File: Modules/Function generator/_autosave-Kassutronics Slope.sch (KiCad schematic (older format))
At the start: 127 parts, among them J1 PJ301M-12, J10 Conn_01x08_Female, J11 Conn_01x08_Male, J12 Conn_01x05_Female, J13 Conn_01x05_Male, J14 Conn_01x06_Female, J15 Conn_01x06_Male, J2 PJ301M-12, J3 PJ301M-12, J4 PJ301M-12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

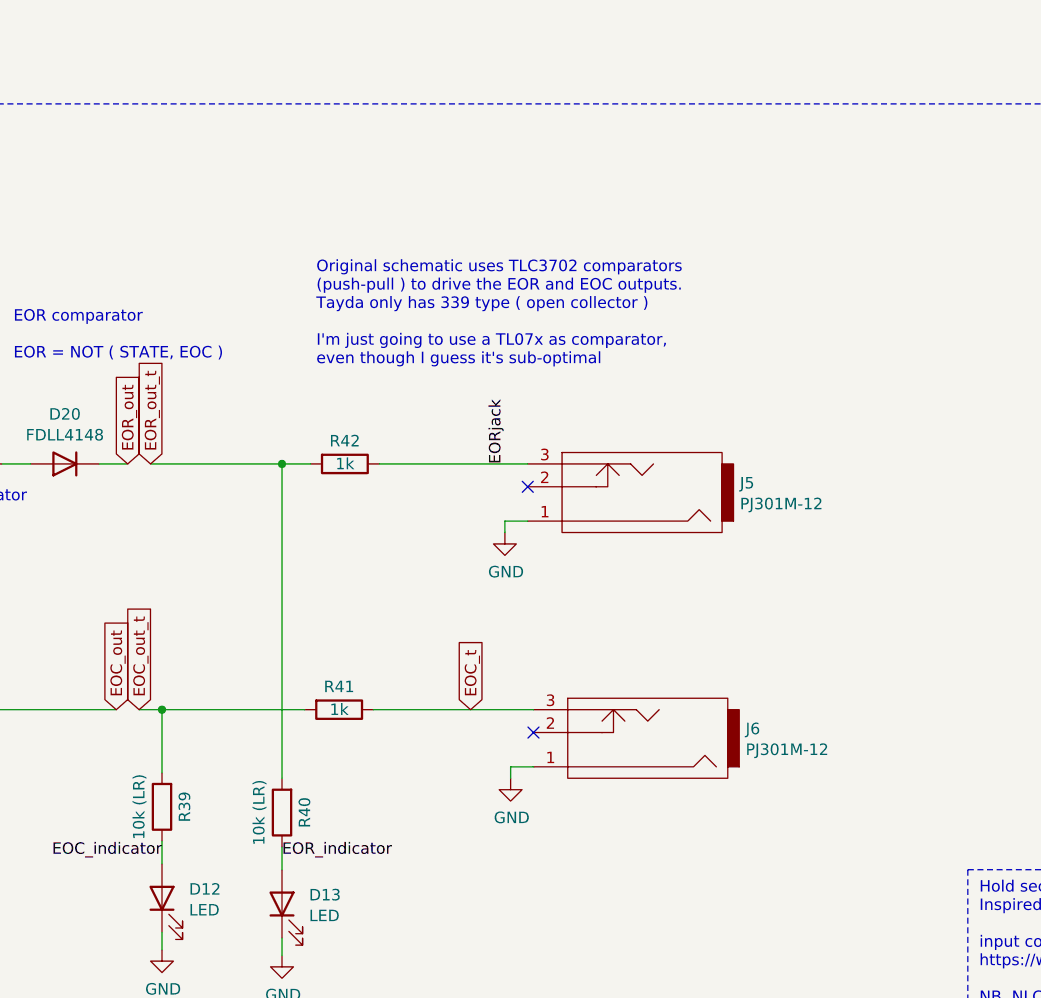
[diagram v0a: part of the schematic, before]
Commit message: Function generator: added pulldown resistors to gate outputs
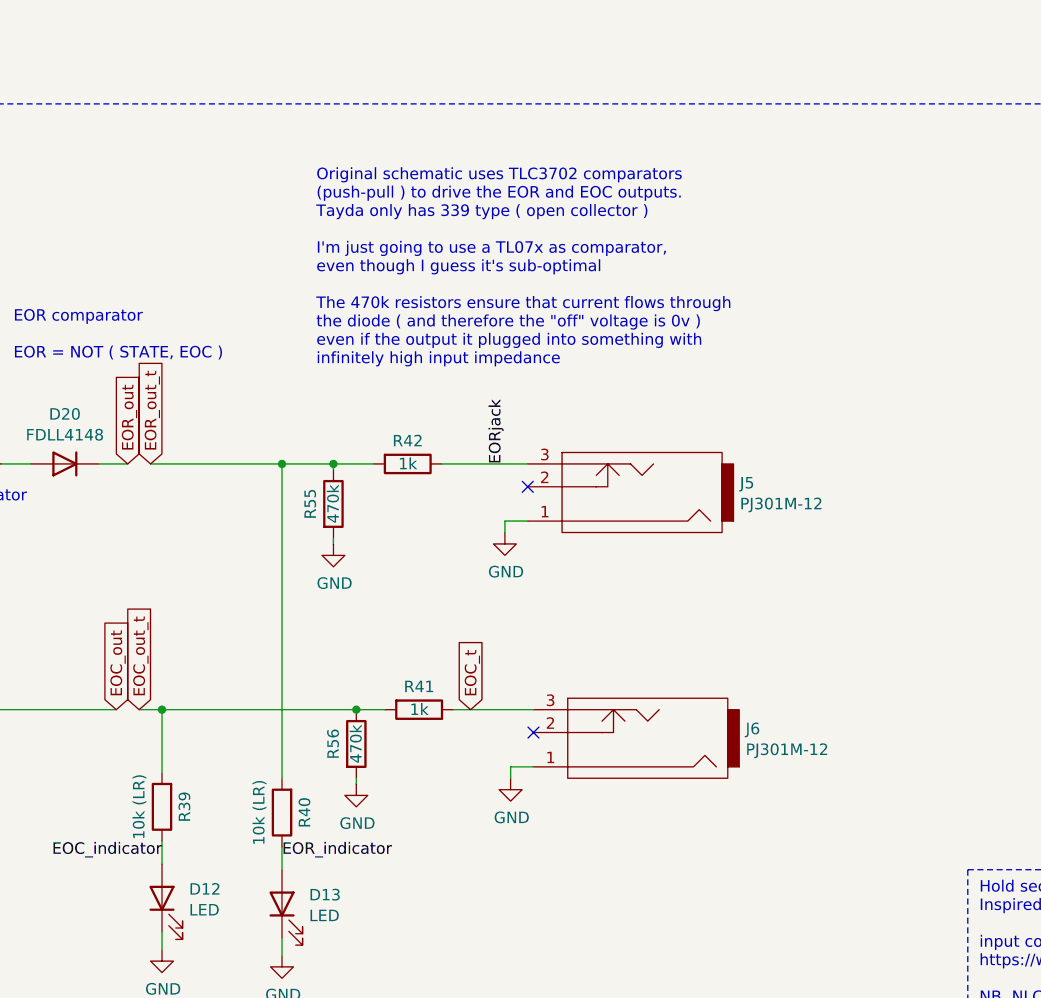
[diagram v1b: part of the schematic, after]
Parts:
- added R55, R56: 470k, Eurocad:R_0805_2012Metric_Pad1.15x1.40mm_HandSolder_smallText, symbol Device:R
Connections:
- net EOC_out_t: now also R56.1
- net EOR_out_t: now also R55.1
- net GND: now also R55.2, R56.2
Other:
- note added: "Original schematic uses TLC3702 comparators \n(push-pull ) to drive the EOR and EOC outputs. \nTayda only has 339 type ( open collector )\n\nI'm just going to use a TL07x as comparator,\neven though I guess it's sub-optimal\n\nThe 470k resistors ensure that current flows through\nthe diode ( and therefore the "off" voltage is 0v ) \neven if the output it plugged into something with\ninfinitely hi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"
- note removed: "Original schematic uses TLC3702 comparators \n(push-pull ) to drive the EOR and EOC outputs. \nTayda only has 339 type ( open collector )\n\nI'm just going to use a TL07x as comparator,\neven though I guess it's sub-optimal"
- moved on the sheet: R41, R42
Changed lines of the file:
@@
 Connection ~ 14550 7975
 Connection ~ 14700 2575
+Connection ~ 14775 7975
+Connection ~ 14875 9050
 Connection ~ 15250 2575
 Connection ~ 15425 2575
@@
 	13975 7975 14550 7975
 Wire Wire Line
-	14025 9050 14650 9050
+	14025 9050 14875 9050
 Wire Wire Line
 	14025 9325 14025 9050
@@
 	14200 3025 13850 3025
 Wire Wire Line
+	14550 7975 14775 7975
+Wire Wire Line
 	14550 9350 14550 7975
 Wire Wire Line
@@
 	14550 10050 14550 10125
 Wire Wire Line
-	14675 7975 14550 7975
-Wire Wire Line
 	14700 2575 14575 2575
 Wire Wire Line
@@
 	14750 2575 14700 2575
 Wire Wire Line
+	14775 7975 14950 7975
+Wire Wire Line
+	14775 8000 14775 7975
+Wire Wire Line
+	14775 8300 14775 8325
+Wire Wire Line
 	14850 13575 14850 13650
 Wire Wire Line
 	14850 14125 14850 14200
 Wire Wire Line
-	14950 9050 15650 9050
-Wire Wire Line
-	14975 7975 15625 7975
+	14875 9050 15000 9050
+Wire Wire Line
+	14875 9350 14875 9375
 Wire Wire Line
 	15050 2575 15250 2575
@@
 Wire Wire Line
 	15250 3300 14450 3300
+Wire Wire Line
+	15250 7975 15625 7975
+Wire Wire Line
+	15300 9050 15650 9050
 Wire Wire Line
 	15400 1450 15450 1450
@@
 I've stuck in some current limiting + capacitage loading compensation\na la dr sketch-n-etch\nhttps://www.muffwiggler.com/forum/viewtopic.php?t=64576\n\nNot 100% sure how the various things connected to "out" will interact with it though
 Text Notes 14700 7550 0    50   ~ 0
-Original schematic uses TLC3702 comparators \n(push-pull ) to drive the EOR and EOC outputs.  \nTayda only has 339 type ( open collector )\n\nI'm just going to use a TL07x as comparator,\neven though I guess it's sub-optimal
+Original schematic uses TLC3702 comparators \n(push-pull ) to drive the EOR and EOC outputs.  \nTayda only has 339 type ( open collector )\n\nI'm just going to use a TL07x as comparator,\neven though I guess it's sub-optimal\n\nThe 470k resistors ensure that current flows through\nthe diode ( and therefore the "off" voltage is 0v ) \neven if the output it plugged into something with\ninfinitely high input impedance
 Text Notes 16275 1325 0    50   ~ 0
 pin 1 is the long lead
@@
 $EndComp
 $Comp
+L power:GND #PWR018
+U 1 1 00000000
+P 14775 8325
+F 0 "#PWR018" H 14775 8075 50  0001 C CNN
+F 1 "GND" H 14780 8152 50  0000 C CNN
+F 2 "" H 14775 8325 50  0001 C CNN
+F 3 "" H 14775 8325 50  0001 C CNN
+	1    14775 8325
+	1    0    0    -1
+$EndComp
+$Comp
+L power:GND #PWR067
+U 1 1 00000000
+P 14875 9375
+F 0 "#PWR067" H 14875 9125 50  0001 C CNN
+F 1 "GND" H 14880 9202 50  0000 C CNN
+F 2 "" H 14875 9375 50  0001 C CNN
+F 3 "" H 14875 9375 50  0001 C CNN
+	1    14875 9375
+	1    0    0    -1
+$EndComp
+$Comp
 L power:GND #PWR034
 U 1 1 6099473E
@@
 $EndComp
 $Comp
-L Device:R R41
-U 1 1 608C89F8
-P 14800 9050
-F 0 "R41" V 14700 9050 50  0000 C CNN
-F 1 "1k" V 14800 9050 50  0000 C CNN
-F 2 "Eurocad:R_0805_2012Metric_Pad1.15x1.40mm_HandSolder_smallText" V 14730 9050 50  0001 C CNN
-F 3 "~" H 14800 9050 50  0001 C CNN
-	1    14800 9050
-	0    1    1    0
-$EndComp
-$Comp
-L Device:R R42
-U 1 1 608C771F
-P 14825 7975
-F 0 "R42" V 14725 7975 50  0000 C CNN
-F 1 "1k" V 14825 7975 50  0000 C CNN
-F 2 "Eurocad:R_0805_2012Metric_Pad1.15x1.40mm_HandSolder_smallText" V 14755 7975 50  0001 C CNN
-F 3 "~" H 14825 7975 50  0001 C CNN
-	1    14825 7975
-	0    1    1    0
+L Device:R R55
+U 1 1 00000000
+P 14775 8150
+F 0 "R55" V 14675 8150 50  0000 C CNN
+F 1 "470k" V 14775 8150 50  0000 C CNN
+F 2 "Eurocad:R_0805_2012Metric_Pad1.15x1.40mm_HandSolder_smallText" V 14705 8150 50  0001 C CNN
+F 3 "~" H 14775 8150 50  0001 C CNN
+	1    14775 8150
+	1    0    0    -1
+$EndComp
+$Comp
+L Device:R R56
+U 1 1 00000000
+P 14875 9200
+F 0 "R56" V 14775 9200 50  0000 C CNN
+F 1 "470k" V 14875 9200 50  0000 C CNN
+F 2 "Eurocad:R_0805_2012Metric_Pad1.15x1.40mm_HandSolder_smallText" V 14805 9200 50  0001 C CNN
+F 3 "~" H 14875 9200 50  0001 C CNN
+	1    14875 9200
+	1    0    0    -1
 $EndComp
 $Comp
@@
 $EndComp
 $Comp
+L Device:R R42
+U 1 1 608C771F
+P 15100 7975
+F 0 "R42" V 15000 7975 50  0000 C CNN
+F 1 "1k" V 15100 7975 50  0000 C CNN
+F 2 "Eurocad:R_0805_2012Metric_Pad1.15x1.40mm_HandSolder_smallText" V 15030 7975 50  0001 C CNN
+F 3 "~" H 15100 7975 50  0001 C CNN
+	1    15100 7975
+	0    1    1    0
+$EndComp
+$Comp
+L Device:R R41
+U 1 1 608C89F8
+P 15150 9050
+F 0 "R41" V 15050 9050 50  0000 C CNN
+F 1 "1k" V 15150 9050 50  0000 C CNN
+F 2 "Eurocad:R_0805_2012Metric_Pad1.15x1.40mm_HandSolder_smallText" V 15080 9050 50  0001 C CNN
+F 3 "~" H 15150 9050 50  0001 C CNN
+	1    15150 9050
+	0    1    1    0
+$EndComp
+$Comp
